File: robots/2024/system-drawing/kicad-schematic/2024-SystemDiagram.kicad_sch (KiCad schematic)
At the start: 207 parts

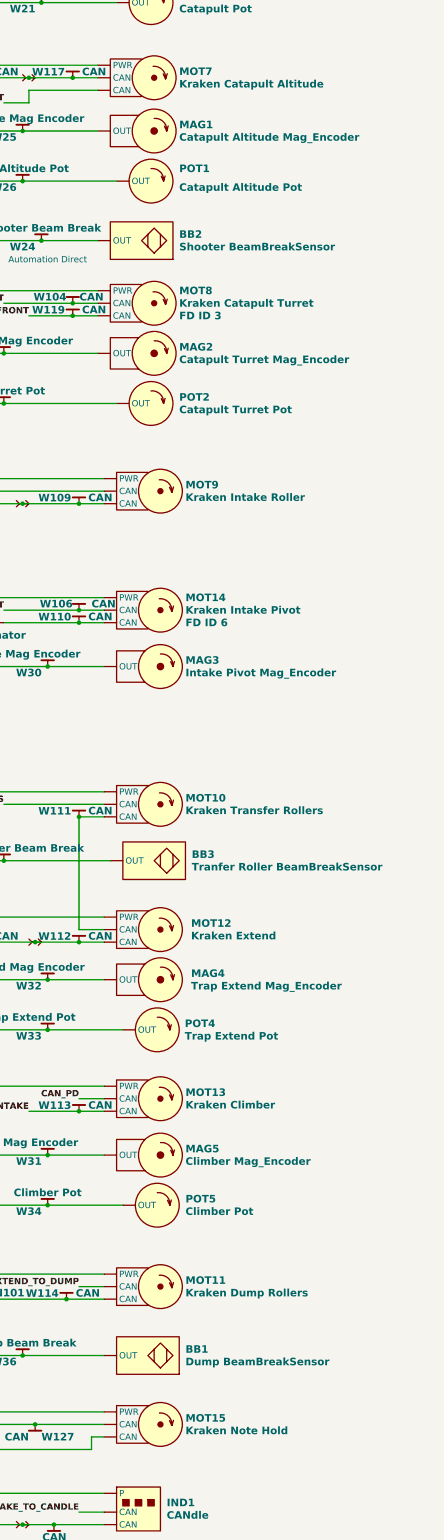
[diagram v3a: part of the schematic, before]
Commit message: Add can ids for remaining motors
Signed-off-by: Scott Berman <sgberman1@gmail.com>
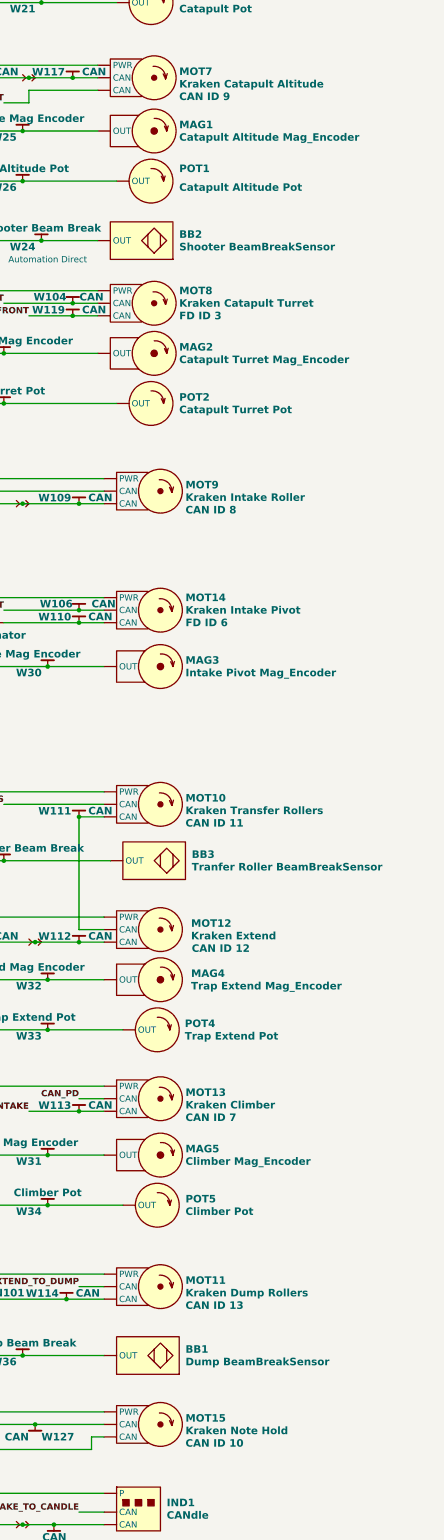
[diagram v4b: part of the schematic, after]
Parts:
- MOT10: CAN ID (none) -> CAN ID 11
- MOT11: CAN ID (none) -> CAN ID 13
- MOT12: CAN ID (none) -> CAN ID 12
- MOT13: CAN ID (none) -> CAN ID 7
- MOT15: CAN ID (none) -> CAN ID 10
- MOT7: CAN ID (none) -> CAN ID 9
- MOT9: CAN ID (none) -> CAN ID 8
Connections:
- net at POE1. (RJ45S): now also RDO1. (POWER); no longer VRM1. (5V/2A)
- net at RDO1. (POWER): now also ETH1. (POWER); no longer VRM1. (5V/2A)
- net at ETH1. (POWER): now also NX1. (Power), W87.; no longer RDO1. (POWER)
- new net: VRM1. (5V/2A), W118., WG1. (4)
- new net: POE1. (RJ45S), VRM1. (5V/2A)
- new net: RDO1. (POWER), VRM1. (5V/2A)
- new net: CAN1. (USB), W67., WG1. (4)
- new net: ETH1. (POWER), NX2. (Power), W88.
- new net: MOT10. (PWR), MOT12. (PWR), W111.
- new net: VRM2. (5V/2A), W85., WG101. (3)
- new net: ETH1. (POWER), VRM2. (5V/2A), W84.
- new net: ETH1. (POWER), NX3. (Power), W89.
- new net: PD2. (IN), WG101. (3)
- new net: MOT1. (PWR), MOT2. (PWR), W105.
- new net: MOT3. (PWR), MOT4. (PWR), W107.
- new net: IMU1. (RIO_PWM2), NX3. (Power), W47.
- now unconnected: VRM2. (5V/2A), VRM2. (5V/2A)
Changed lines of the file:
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@@
   )
   (symbol (lib_id "SystemDiagram:Falcon_Motor") (at 609.6 426.72 0) (unit 1)
-    (in_bom yes) (on_board yes) (dnp no) (fields_autoplaced)
+    (in_bom yes) (on_board yes) (dnp no)
     (property "Reference" "MOT11" (at 623.57 425.45 0)
       (effects (font (face "FreeSans") (size 1.524 1.524) bold) (justify left))
@@
       (effects (font (size 1.27 1.27)) hide)
     )
+    (property "CAN ID" "CAN ID 13" (at 623.57 430.53 0)
+      (effects (font (face "FreeSans") (size 1.524 1.524) bold) (justify left))
+    )
     (pin "")
     (pin "")
@@
   )
   (symbol (lib_id "SystemDiagram:Falcon_Motor") (at 609.6 354.33 0) (unit 1)
-    (in_bom yes) (on_board yes) (dnp no) (fields_autoplaced)
+    (in_bom yes) (on_board yes) (dnp no)
     (property "Reference" "MOT12" (at 624.6989 353.06 0)
       (effects (font (face "FreeSans") (size 1.524 1.524) bold) (justify left))
@@
       (effects (font (size 1.27 1.27)) hide)
     )
+    (property "CAN ID" "CAN ID 12" (at 624.84 358.14 0)
+      (effects (font (face "FreeSans") (size 1.524 1.524) bold) (justify left))
+    )
     (pin "")
     (pin "")
@@
   )
   (symbol (lib_id "SystemDiagram:Falcon_Motor") (at 609.6 328.93 0) (unit 1)
-    (in_bom yes) (on_board yes) (dnp no) (fields_autoplaced)
+    (in_bom yes) (on_board yes) (dnp no)
     (property "Reference" "MOT10" (at 623.57 327.66 0)
       (effects (font (face "FreeSans") (size 1.524 1.524) bold) (justify left))
@@
       (effects (font (size 1.27 1.27)) hide)
     )
+    (property "CAN ID" "CAN ID 11" (at 623.57 332.74 0)
+      (effects (font (face "FreeSans") (size 1.524 1.524) bold) (justify left))
+    )
     (pin "")
     (pin "")
@@
   )
   (symbol (lib_id "SystemDiagram:Falcon_Motor") (at 609.6 454.66 0) (unit 1)
-    (in_bom yes) (on_board yes) (dnp no) (fields_autoplaced)
+    (in_bom yes) (on_board yes) (dnp no)
     (property "Reference" "MOT15" (at 623.57 453.39 0)
       (effects (font (face "FreeSans") (size 1.524 1.524) bold) (justify left))
@@
       (effects (font (size 1.27 1.27)) hide)
     )
+    (property "CAN ID" "CAN ID 10" (at 623.57 458.47 0)
+      (effects (font (face "FreeSans") (size 1.524 1.524) bold) (justify left))
+    )
     (pin "")
     (pin "")
@@
   )
   (symbol (lib_id "SystemDiagram:Falcon_Motor") (at 609.6 265.43 0) (unit 1)
-    (in_bom yes) (on_board yes) (dnp no) (fields_autoplaced)
+    (in_bom yes) (on_board yes) (dnp no)
     (property "Reference" "MOT9" (at 623.57 264.16 0)
       (effects (font (face "FreeSans") (size 1.524 1.524) bold) (justify left))
@@
       (effects (font (size 1.27 1.27)) hide)
     )
-    (property "CAN ID" "" (at 609.6 265.43 0)
-      (effects (font (size 1.27 1.27)))
+    (property "CAN ID" "CAN ID 8" (at 623.57 269.24 0)
+      (effects (font (face "FreeSans") (size 1.524 1.524) bold) (justify left))
     )
     (pin "")
@@
   )
   (symbol (lib_id "SystemDiagram:Falcon_Motor") (at 608.33 181.61 0) (unit 1)
-    (in_bom yes) (on_board yes) (dnp no) (fields_autoplaced)
+    (in_bom yes) (on_board yes) (dnp no)
     (property "Reference" "MOT7" (at 622.3 180.34 0)
       (effects (font (face "FreeSans") (size 1.524 1.524) bold) (justify left))
@@
       (effects (font (size 1.27 1.27)) hide)
     )
+    (property "CAN ID" "CAN ID 9" (at 622.3 185.42 0)
+      (effects (font (face "FreeSans") (size 1.524 1.524) bold) (justify left))
+    )
     (pin "")
     (pin "")
@@
   )
   (symbol (lib_id "SystemDiagram:Falcon_Motor") (at 609.6 388.62 0) (unit 1)
-    (in_bom yes) (on_board yes) (dnp no) (fields_autoplaced)
+    (in_bom yes) (on_board yes) (dnp no)
     (property "Reference" "MOT13" (at 623.57 387.35 0)
       (effects (font (face "FreeSans") (size 1.524 1.524) bold) (justify left))
@@
       (effects (font (size 1.27 1.27)) hide)
     )
+    (property "CAN ID" "CAN ID 7" (at 623.57 392.43 0)
+      (effects (font (face "FreeSans") (size 1.524 1.524) bold) (justify left))
+    )
     (pin "")

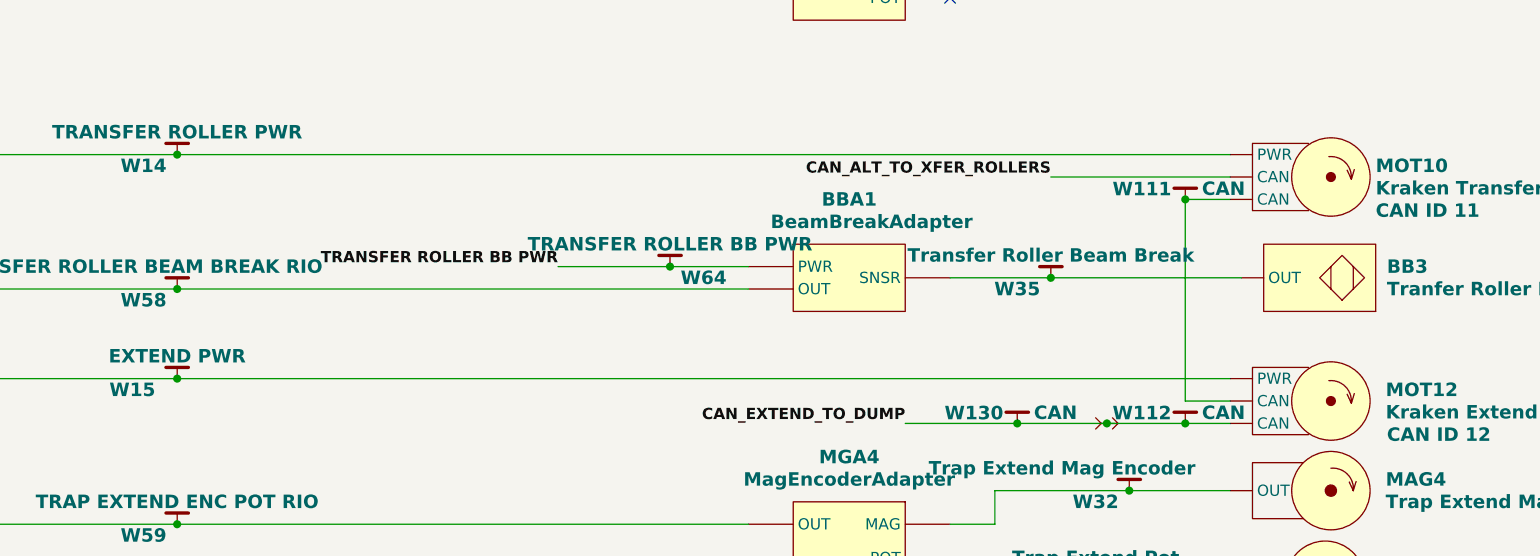
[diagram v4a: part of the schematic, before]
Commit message: Change transfer roller beam break circuit to DNP
Signed-off-by: Scott Berman <sgberman1@gmail.com>
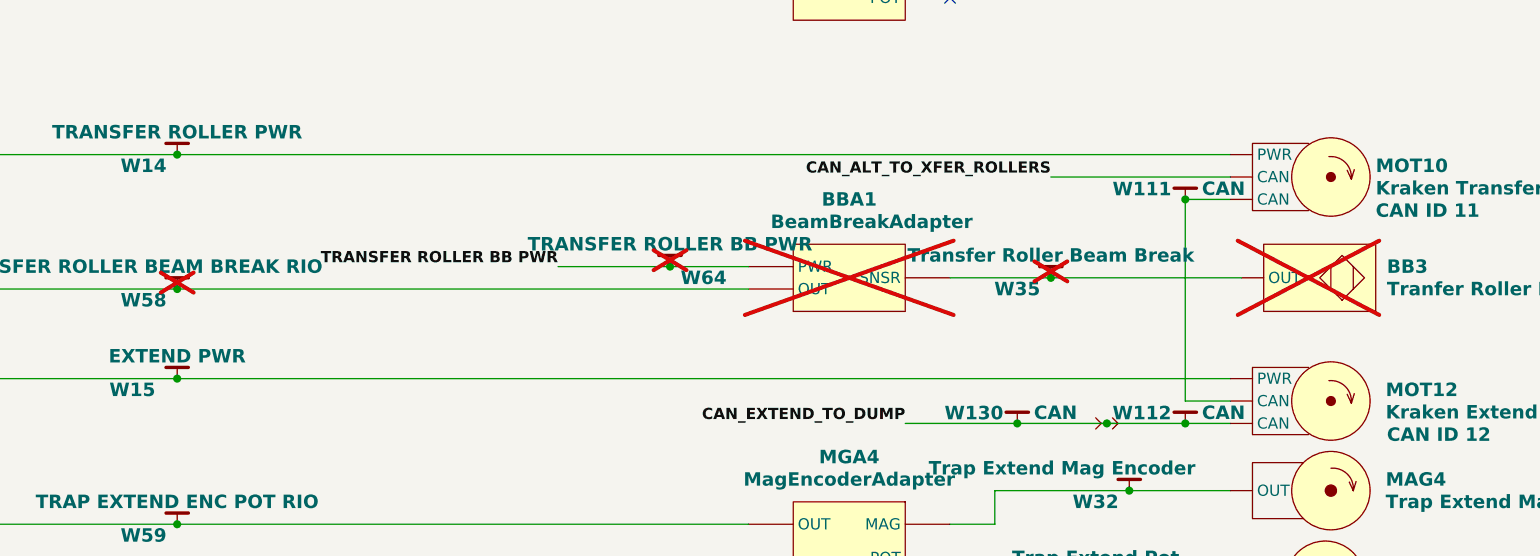
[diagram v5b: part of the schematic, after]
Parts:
- BB3, BBA1, W35, W58, W64: now not fitted
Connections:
- net at POE1. (RJ45S): now also RDO1. (POWER); no longer VRM1. (5V/2A)
- net at RDO1. (POWER): now also ETH1. (POWER); no longer VRM1. (5V/2A)
- net at ETH1. (POWER): now also NX1. (Power), W87.; no longer RDO1. (POWER)
- new net: VRM1. (5V/2A), W118., WG1. (4)
- new net: POE1. (RJ45S), VRM1. (5V/2A)
- new net: RDO1. (POWER), VRM1. (5V/2A)
- new net: CAN1. (USB), W67., WG1. (4)
- new net: ETH1. (POWER), NX2. (Power), W88.
- new net: MOT10. (PWR), MOT12. (PWR), W111.
- new net: VRM2. (5V/2A), W85., WG101. (3)
- new net: ETH1. (POWER), VRM2. (5V/2A), W84.
- new net: ETH1. (POWER), NX3. (Power), W89.
- new net: PD2. (IN), WG101. (3)
- new net: MOT1. (PWR), MOT2. (PWR), W105.
- new net: MOT3. (PWR), MOT4. (PWR), W107.
- new net: IMU1. (RIO_PWM2), NX3. (Power), W47.
- now unconnected: VRM2. (5V/2A), VRM2. (5V/2A)
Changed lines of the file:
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@@
   )
   (symbol (lib_id "SystemDiagram:WireTag") (at 586.74 340.36 0) (unit 1)
-    (in_bom yes) (on_board yes) (dnp no)
+    (in_bom yes) (on_board yes) (dnp yes)
     (property "Reference" "W35" (at 582.93 341.63 0)
       (effects (font (face "FreeSans") (size 1.524 1.524) bold))
@@
   )
   (symbol (lib_id "SystemDiagram:WireTag") (at 487.68 341.63 0) (unit 1)
-    (in_bom yes) (on_board yes) (dnp no)
+    (in_bom yes) (on_board yes) (dnp yes)
     (property "Reference" "W58" (at 483.87 342.9 0)
       (effects (font (face "FreeSans") (size 1.524 1.524) bold))
@@
   )
   (symbol (lib_id "SystemDiagram:WireTag") (at 543.56 339.09 0) (unit 1)
-    (in_bom yes) (on_board yes) (dnp no)
+    (in_bom yes) (on_board yes) (dnp yes)
     (property "Reference" "W64" (at 547.37 340.36 0)
       (effects (font (face "FreeSans") (size 1.524 1.524) bold))
@@
   )
   (symbol (lib_id "SystemDiagram:BeamBreakSensor") (at 623.57 344.17 180) (unit 1)
-    (in_bom yes) (on_board yes) (dnp no) (fields_autoplaced)
+    (in_bom yes) (on_board yes) (dnp yes) (fields_autoplaced)
     (property "Reference" "BB3" (at 624.84 339.09 0)
       (effects (font (face "FreeSans") (size 1.524 1.524) bold) (justify right))
@@
   )
   (symbol (lib_id "SystemDiagram:BeamBreakAdapter") (at 557.53 336.55 0) (unit 1)
-    (in_bom yes) (on_board yes) (dnp no)
+    (in_bom yes) (on_board yes) (dnp yes)
     (property "Reference" "BBA1" (at 563.88 331.47 0)
       (effects (font (face "FreeSans") (size 1.524 1.524) bold))
